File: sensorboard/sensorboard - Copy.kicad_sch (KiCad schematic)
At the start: 66 parts, among them J10 Conn_01x02_Male, J11 Conn_01x05_Male, J9 Conn_01x02_Male, Q1 MMDT2222A, U1 ESP32-PICO-D4, U2 LTC4411, U3 TPS61092RSAR

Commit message: rearrange CAN, USB port and new copies
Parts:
- C1, C2, C3: value 1nF -> 0.1uF
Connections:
- net C55 is gone; now on net CS5: TP11.1, U1.20 (IO13)
- net BOOT: now also TP9.1, U1.29 (SD3/IO10); no longer TP8.1, U1.23 (IO0)
- net CAN_RX: now also TP22.1, U1.25 (IO16); no longer TP23.1, U1.13 (IO33)
- net CAN_TX: now also TP23.1, U1.27 (IO17); no longer TP22.1, U1.12 (IO32)
- net CS0: now also TP8.1, U1.23 (IO0); no longer TP21.1, U1.16 (IO27)
- net CS2: now also TP2.1, U1.24 (IO4); no longer TP19.1, U1.14 (IO25)
- net CS3: now also TP1.1, U1.22 (IO2); no longer TP13.1, U1.21 (IO15)
- net CS4: now also TP13.1, U1.21 (IO15); no longer TP12.1, U1.17 (IO14)
- net CS6: now also TP21.1, U1.16 (IO27); no longer TP10.1, U1.18 (IO12)
- net CS7: now also TP10.1, U1.18 (IO12); no longer TP9.1, U1.29 (SD3/IO10)
- net CS8: now also TP19.1, U1.14 (IO25); no longer TP2.1, U1.28 (SD2/IO9)
- net CS9: now also TP12.1, U1.17 (IO14); no longer TP1.1, U1.34 (IO5)
- net LED: now also U1.34 (IO5); no longer U1.22 (IO2)
- no-connect marks 35 -> 37
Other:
- moved on the sheet: TP1, TP2, TP22, TP23

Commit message: Change 3.3V, added curved edges
changed the copy, added keepout for UFL connector
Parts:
- removed ANT1: AMCA31-2R450G-S1F-T3, iclr:ANT_AMCA31-2R450G-S1F-T3, symbol AMCA31-2R450G-S1F-T3:AMCA31-2R450G-S1F-T3
- removed C4: 1.2pF, Capacitor_SMD:C_0603_1608Metric, symbol Device:C_Small
- removed C5: 1.5pF, Capacitor_SMD:C_0603_1608Metric, symbol Device:C_Small
- removed L2: LQG15WZ1N8B02D, iclr:INDC1006X60N, symbol Device:L
- added J15: Conn_Coaxial, Connector_Coaxial:U.FL_Molex_MCRF_73412-0110_Vertical, symbol Connector:Conn_Coaxial
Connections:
- net +3V3: now also C13.1
- net +5V: now also C15.1
- net GND: now also J15.2 (Ext)
- net LED: now also U1.12 (IO32); no longer U1.34 (IO5)
- net LNA_IN: now also J15.1 (In)

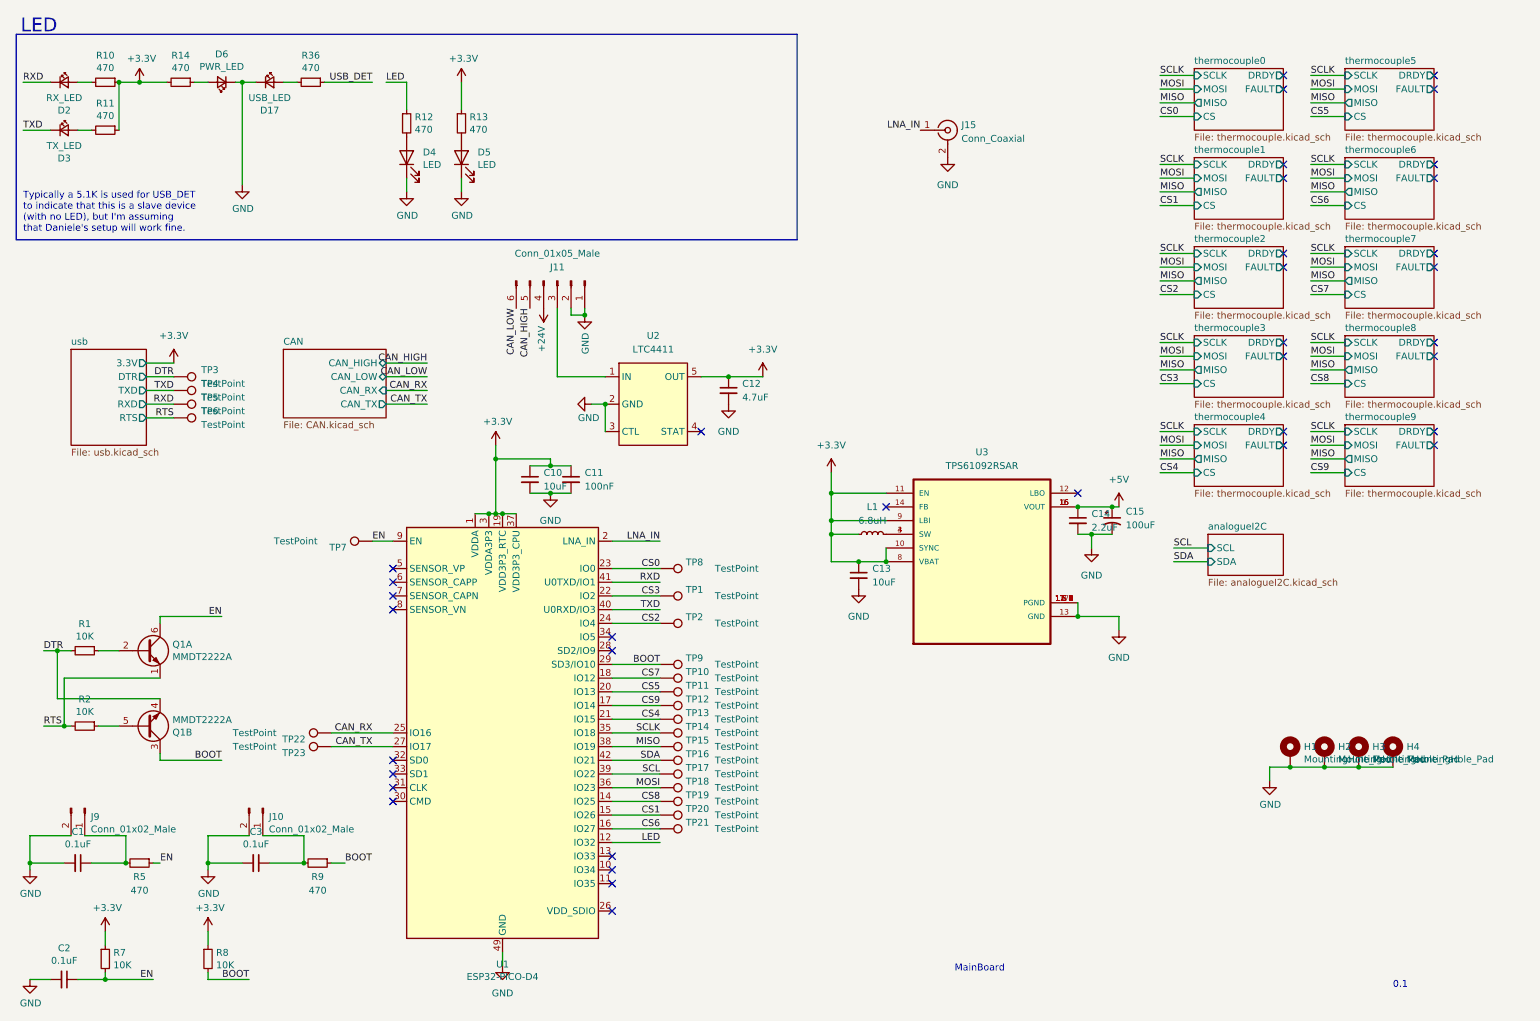
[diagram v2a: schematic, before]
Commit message: fixed CS lines
before cleanup
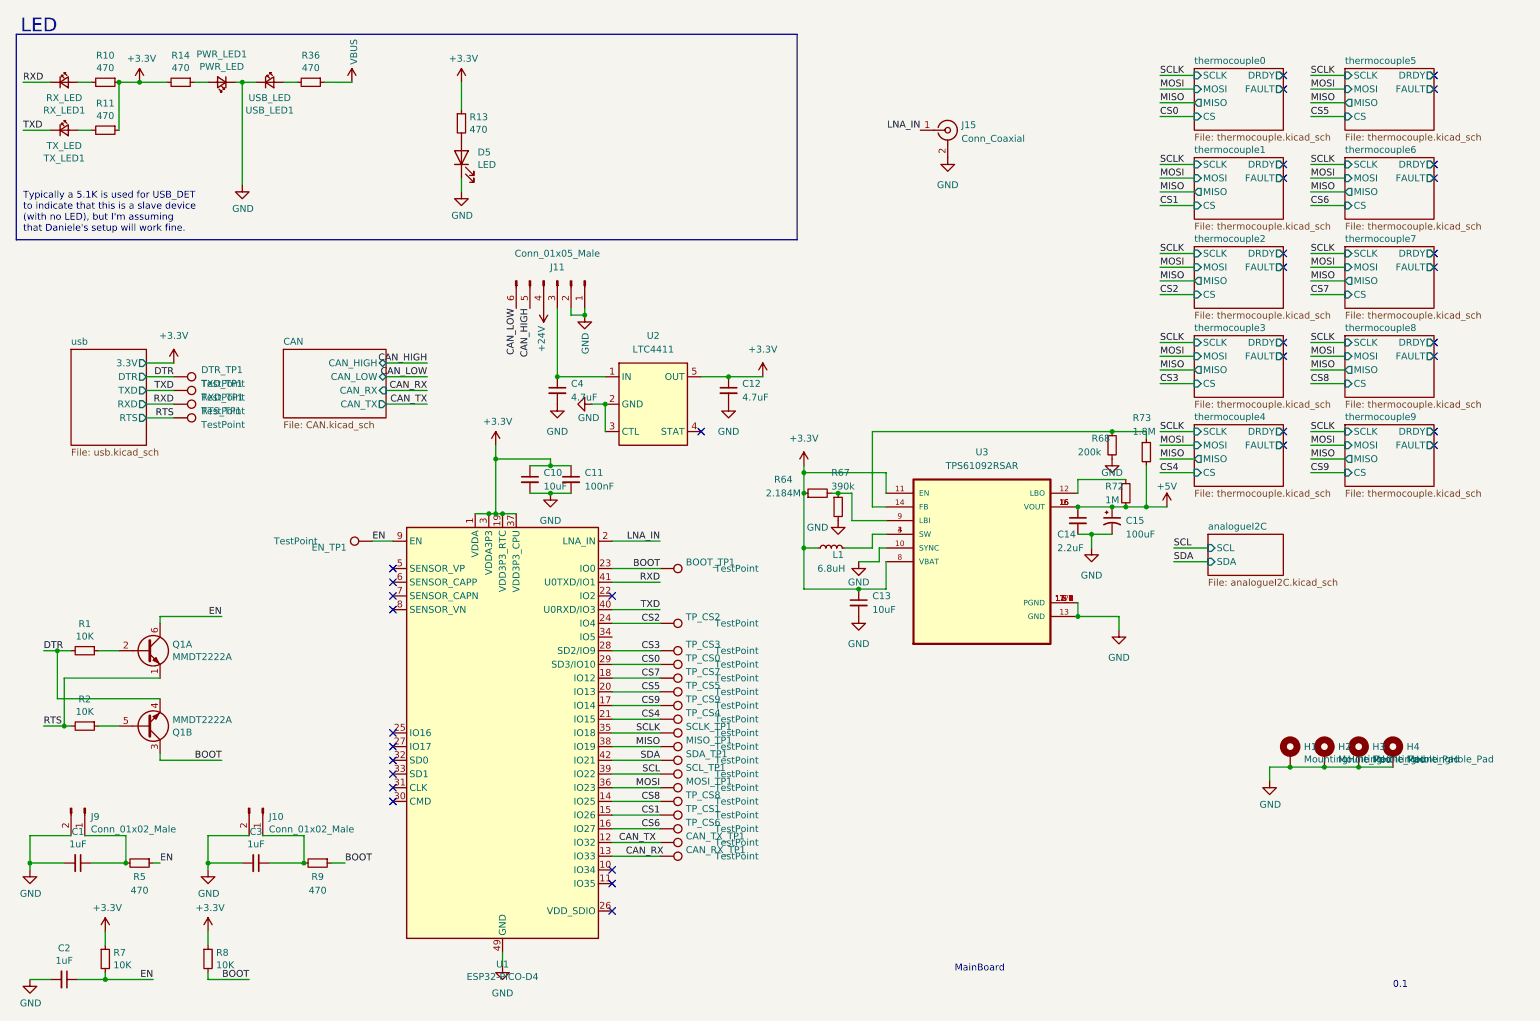
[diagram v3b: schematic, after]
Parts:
- removed D4: LED, LED_SMD:LED_0603_1608Metric, symbol Device:LED
- removed R12: 470, Resistor_SMD:R_0603_1608Metric, symbol Device:R_Small
- added C4: 4.7uF, Capacitor_SMD:C_0603_1608Metric, symbol Device:C_Small
- added R64: 2.184M, Resistor_SMD:R_0603_1608Metric, symbol Device:R_Small
- added R67: 390k, Resistor_SMD:R_0603_1608Metric, symbol Device:R_Small
- added R68: 200k, Resistor_SMD:R_0603_1608Metric, symbol Device:R_Small
- added R72: 1M, Resistor_SMD:R_0603_1608Metric, symbol Device:R_Small
- added R73: 1.8M, Resistor_SMD:R_0603_1608Metric, symbol Device:R_Small
- C1, C2, C3: value 0.1uF -> 1uF
- C15: footprint Capacitor_SMD:C_0603_1608Metric -> iclr:CAPC2012X145N
- L1: footprint iclr:INDC1006X60N -> iclr:INDPM3030X200N
- renumbered TP9 to BOOT_TP1, TP22 to CAN_RX_TP1, TP23 to CAN_TX_TP1, TP3 to DTR_TP1, TP7 to EN_TP1, TP15 to MISO_TP1, TP18 to MOSI_TP1, D6 to PWR_LED1, TP6 to RTS_TP1, TP5 to RXD_TP1, D2 to RX_LED1, TP14 to SCLK_TP1, TP17 to SCL_TP1, TP16 to SDA_TP1, TP8 to TP_CS0, TP20 to TP_CS1, TP2 to TP_CS2, TP1 to TP_CS3, TP13 to TP_CS4, TP11 to TP_CS5, TP21 to TP_CS6, TP10 to TP_CS7, TP19 to TP_CS8, TP12 to TP_CS9, TP4 to TXD_TP1, D3 to TX_LED1, D17 to USB_LED1
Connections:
- net LED is gone; now on net CAN_TX: U1.12 (IO32)
- net +3V3: now also R64.1; no longer U3.10 (SYNC), U3.9 (LBI)
- net +5V: now also R72.2, R73.2
- net BOOT: now also U1.23 (IO0); no longer U1.29 (SD3/IO10)
- net CAN_RX: now also U1.13 (IO33); no longer U1.25 (IO16)
- net CAN_TX: no longer U1.27 (IO17)
- net CS0: now also U1.29 (SD3/IO10); no longer U1.23 (IO0)
- net CS3: now also U1.28 (SD2/IO9); no longer U1.22 (IO2)
- net GND: now also U3.10 (SYNC), C4.2, R67.2, R68.2
- net at J11.3 (Pin_3), U2.1 (IN): now also C4.1
- net at U3.12 (LBO): now also R72.1
- net at U3.14 (FB): now also R68.1, R73.1
- net USB_DET renamed VBUS
- new net: R64.2, R67.1, U3.9 (LBI)
- no-connect marks 37 -> 35
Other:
- moved on the sheet: BOOT_TP1, C13, CAN_RX_TP1, CAN_TX_TP1, L1, TP_CS0, TP_CS3
